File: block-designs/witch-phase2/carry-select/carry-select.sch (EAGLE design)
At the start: 12 parts, among them IC1 74AHC1G32DBV, IC2 74AHC1G08DBV, IC3 74175-S

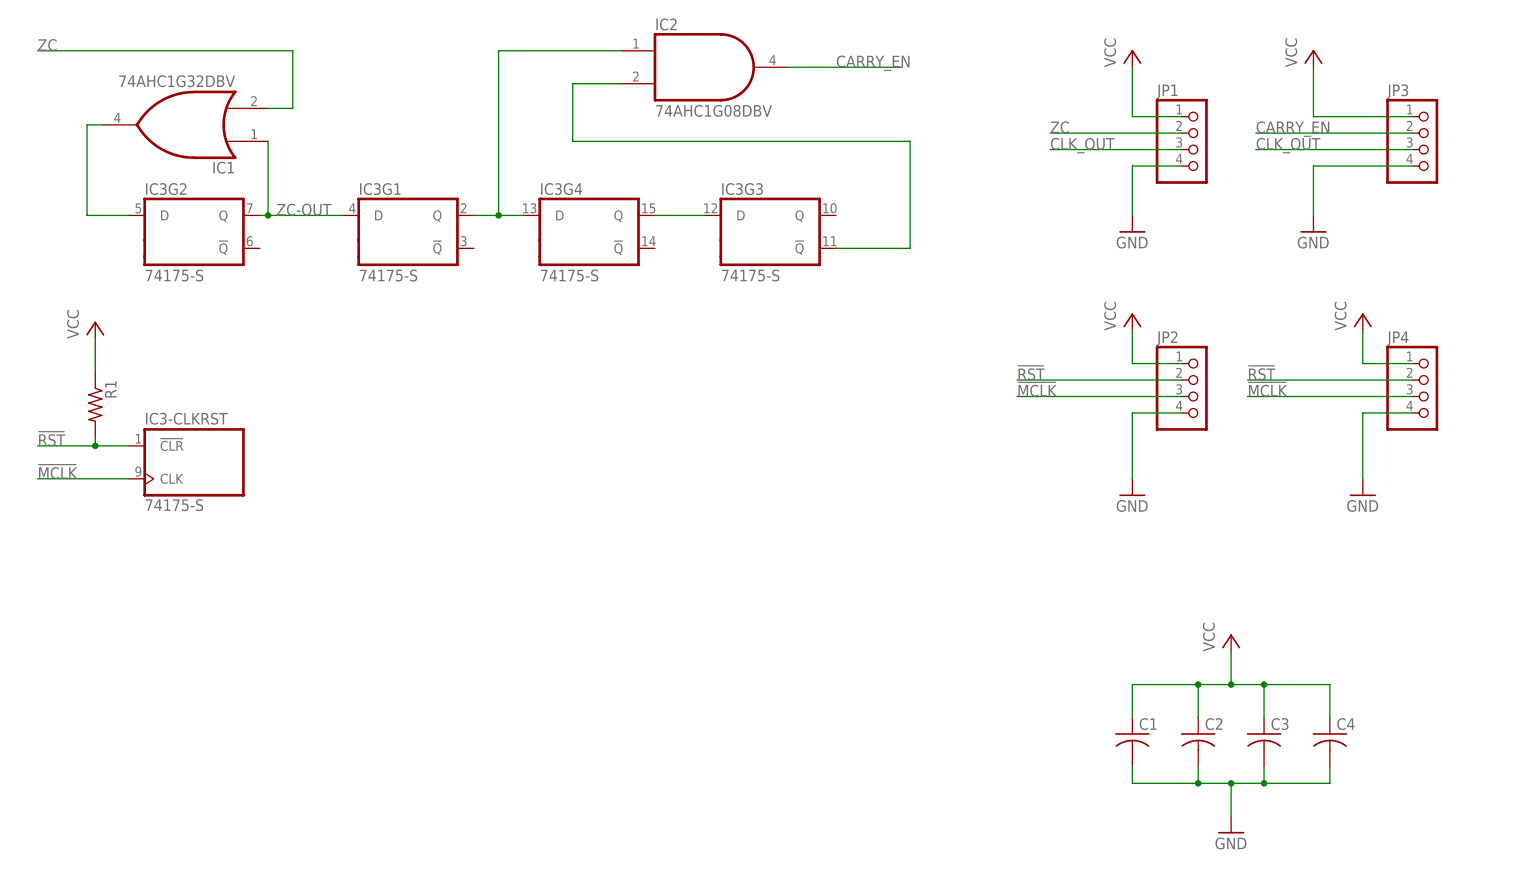
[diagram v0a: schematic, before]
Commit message: break the carry section into two pcbs and add new flipflop design
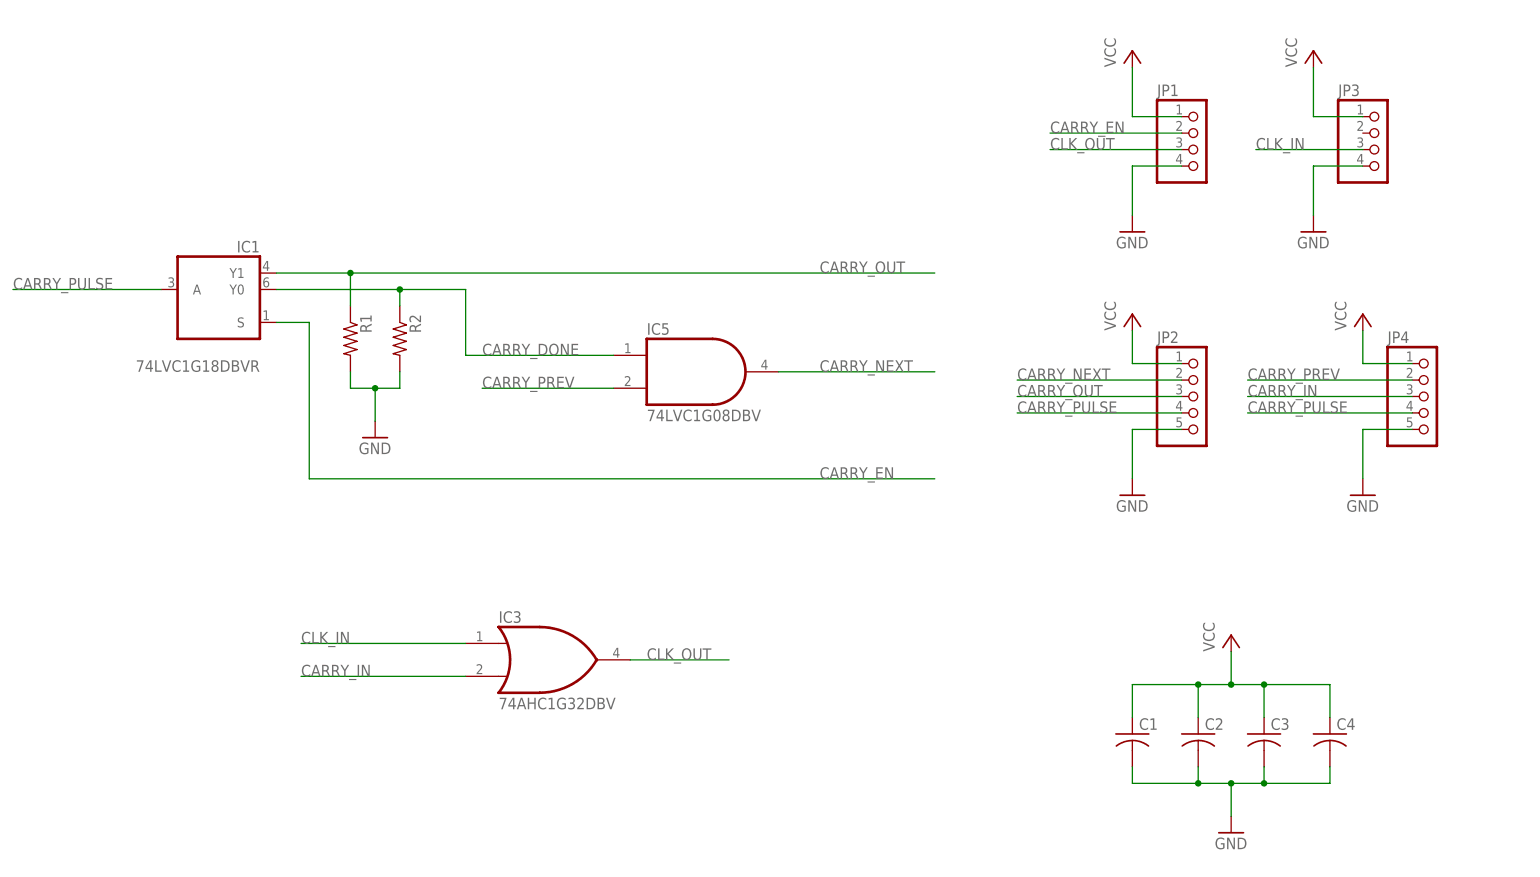
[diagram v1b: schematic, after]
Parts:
- removed IC2: 74AHC1G08DBV, 74xx-little-us:74AHC1G08DBV
- added IC5: 74LVC1G08DBV, 74xx-little-us:74LVC1G08DBV
- added R2: (no value), resistor:R-US_R0805
- IC1: value 74AHC1G32DBV -> 74LVC1G18DBVR; device 74xx-little-us:74AHC1G32DBV -> 74xx-little-us:741G18
- IC3: value 74175-S -> 74AHC1G32DBV; device 74xx-us:74175-S -> 74xx-little-us:74AHC1G32DBV
- JP2, JP4: device pinhead:PINHD-1X4 -> pinhead:PINHD-1X5
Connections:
- removed net !MCLK: IC3-CLKRST.CLK, JP2.3, JP4.3
- removed net !RST: IC3-CLKRST.!CLR, JP2.2, JP4.2, R1.2
- removed net N$1: IC2A.I0, IC3G1.Q, IC3G4.D
- removed net N$2: IC2A.I1, IC3G3.!Q
- removed net N$3: IC3G3.D, IC3G4.Q
- removed net N$5: IC1A.O, IC3G2.D
- removed net ZC: IC1A.I1, JP1.2
- removed net ZC-OUT: IC1A.I0, IC3G1.D, IC3G2.Q
- new net CARRY_DONE: IC1G$1.Y0, IC5A.I0, R2.1
- new net CARRY_IN: IC3A.I1, JP4.3
- new net CARRY_NEXT: IC5A.O, JP2.2
- new net CARRY_OUT: IC1G$1.Y1, JP2.3, R1.1
- new net CARRY_PREV: IC5A.I1, JP4.2
- new net CARRY_PULSE: IC1G$1.A, JP2.4, JP4.4
- new net CLK_IN: IC3A.I0, JP3.3
- net CARRY_EN: now also IC1G$1.S, JP1.2; no longer IC2A.O, JP3.2
- net CLK_OUT: now also IC3A.O; no longer JP3.3
- net GND: now also JP2.5, JP4.5, R1.2, R2.2; no longer JP2.4, JP4.4
- net VCC: no longer R1.1
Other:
- moved on the sheet: JP3, R1

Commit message: updated designs for new labeling and spacing
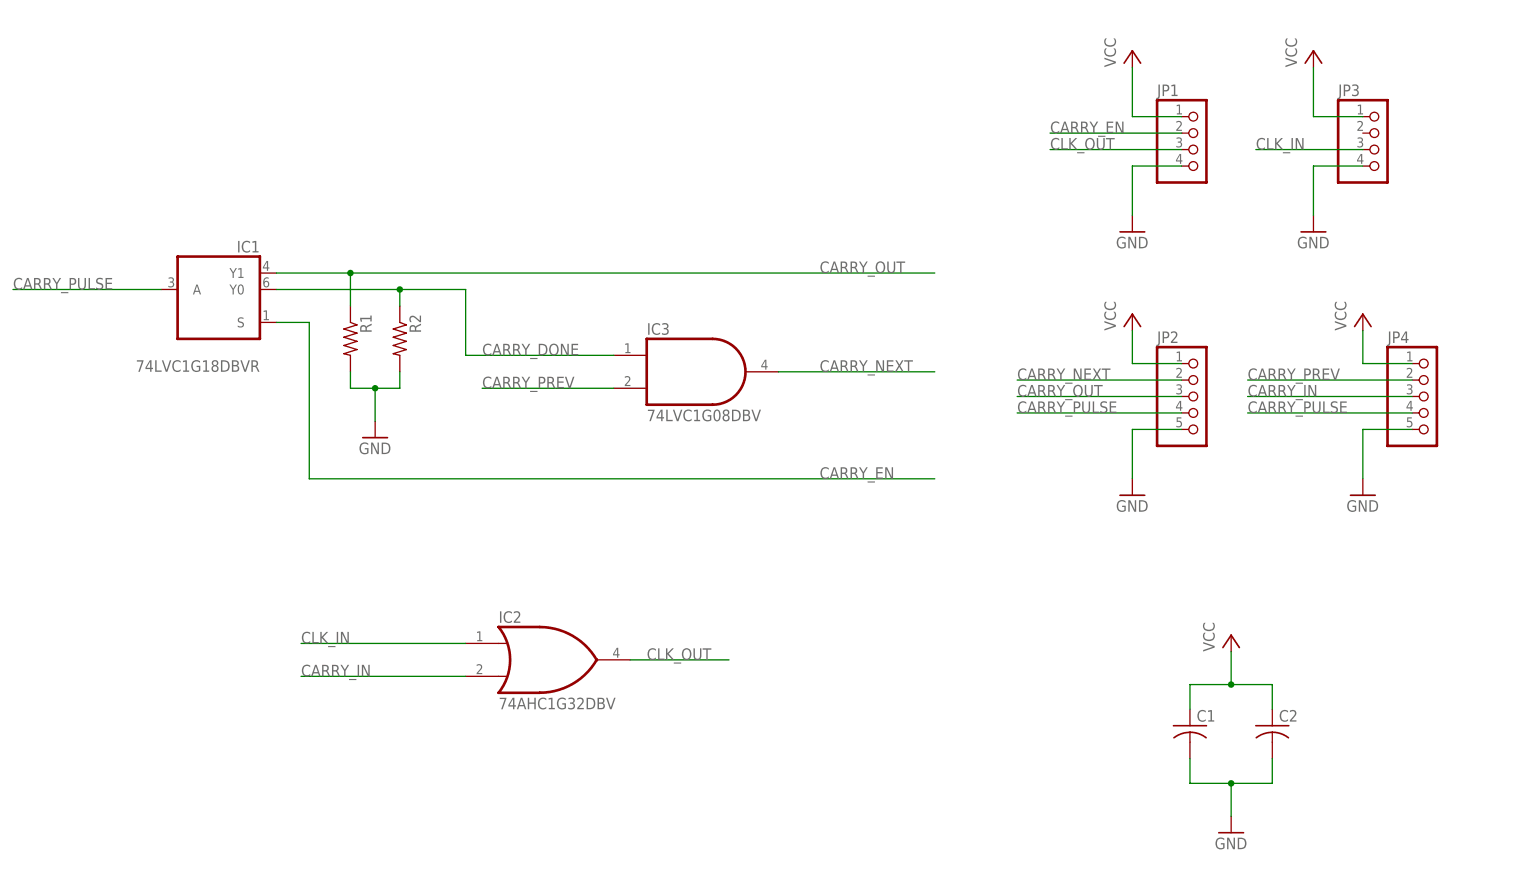
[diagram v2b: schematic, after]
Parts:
- removed C3, C4: (no value), resistor:C-USC0805
- removed IC5: 74LVC1G08DBV, 74xx-little-us:74LVC1G08DBV
- added IC2: 74AHC1G32DBV, 74xx-little-us:74AHC1G32DBV
- IC3: value 74AHC1G32DBV -> 74LVC1G08DBV; device 74xx-little-us:74AHC1G32DBV -> 74xx-little-us:74LVC1G08DBV
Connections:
- net CARRY_DONE: now also IC3A.I0; no longer IC5A.I0
- net CARRY_IN: now also IC2A.I1; no longer IC3A.I1
- net CARRY_NEXT: now also IC3A.O; no longer IC5A.O
- net CARRY_PREV: now also IC3A.I1; no longer IC5A.I1
- net CLK_IN: now also IC2A.I0; no longer IC3A.I0
- net CLK_OUT: now also IC2A.O; no longer IC3A.O
- net GND: no longer C3.2, C4.2
- net VCC: no longer C3.1, C4.1
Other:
- moved on the sheet: C1, C2
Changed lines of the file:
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@@
 <setting verticaltext="up"/>
 </settings>
-<grid distance="0.05" unitdist="inch" unit="inch" style="dots" multiple="1" display="no" altdistance="0.01" altunitdist="inch" altunit="inch"/>
+<grid distance="0.1" unitdist="inch" unit="inch" style="dots" multiple="1" display="no" altdistance="0.01" altunitdist="inch" altunit="inch"/>
 <layers>
 <layer number="1" name="Top" color="4" fill="1" visible="no" active="no"/>
@@
 <part name="GND5" library="supply1" deviceset="GND" device=""/>
 <part name="C1" library="resistor" deviceset="C-US" device="C0805"/>
+<part name="GND4" library="supply1" deviceset="GND" device=""/>
 <part name="C2" library="resistor" deviceset="C-US" device="C0805"/>
-<part name="C3" library="resistor" deviceset="C-US" device="C0805"/>
-<part name="GND4" library="supply1" deviceset="GND" device=""/>
-<part name="C4" library="resistor" deviceset="C-US" device="C0805"/>
 <part name="FRAME1" library="frames" deviceset="LETTER_L" device=""/>
 <part name="JP1" library="pinhead" deviceset="PINHD-1X4" device=""/>
@@
 <part name="JP4" library="pinhead" deviceset="PINHD-1X5" device=""/>
 <part name="IC1" library="74xx-little-us" deviceset="74*1G18" device="" value="74LVC1G18DBVR"/>
+<part name="P+3" library="supply1" deviceset="VCC" device=""/>
+<part name="P+1" library="supply1" deviceset="VCC" device=""/>
 <part name="P+4" library="supply1" deviceset="VCC" device=""/>
-<part name="P+2" library="supply1" deviceset="VCC" device=""/>
-<part name="P+5" library="supply1" deviceset="VCC" device=""/>
 <part name="R1" library="resistor" deviceset="R-US_" device="R0805"/>
 <part name="R2" library="resistor" deviceset="R-US_" device="R0805"/>
 <part name="GND1" library="supply1" deviceset="GND" device=""/>
-<part name="P+6" library="supply1" deviceset="VCC" device=""/>
-<part name="P+3" library="supply1" deviceset="VCC" device=""/>
-<part name="IC3" library="74xx-little-us" deviceset="74*1G32" device="DBV" technology="AHC"/>
-<part name="IC5" library="74xx-little-us" deviceset="74*1G08" device="DBV" technology="LVC"/>
+<part name="P+5" library="supply1" deviceset="VCC" device=""/>
+<part name="P+2" library="supply1" deviceset="VCC" device=""/>
+<part name="IC2" library="74xx-little-us" deviceset="74*1G32" device="DBV" technology="AHC"/>
+<part name="IC3" library="74xx-little-us" deviceset="74*1G08" device="DBV" technology="LVC"/>
 </parts>
 <sheets>
@@
 <instance part="GND6" gate="1" x="214.63" y="107.95"/>
 <instance part="GND5" gate="1" x="207.01" y="148.59"/>
-<instance part="C1" gate="G$1" x="179.07" y="71.12"/>
-<instance part="C2" gate="G$1" x="189.23" y="71.12"/>
-<instance part="C3" gate="G$1" x="199.39" y="71.12"/>
+<instance part="C1" gate="G$1" x="187.96" y="72.39"/>
 <instance part="GND4" gate="1" x="194.31" y="55.88"/>
-<instance part="C4" gate="G$1" x="209.55" y="71.12"/>
+<instance part="C2" gate="G$1" x="200.66" y="72.39"/>
 <instance part="FRAME1" gate="G$1" x="0" y="0"/>
 <instance part="FRAME1" gate="G$2" x="147.32" y="0"/>
@@
 <instance part="JP4" gate="A" x="224.79" y="123.19"/>
 <instance part="IC1" gate="G$1" x="38.1" y="138.43" rot="MR0"/>
-<instance part="P+4" gate="VCC" x="194.31" y="86.36"/>
-<instance part="P+2" gate="VCC" x="179.07" y="176.53"/>
-<instance part="P+5" gate="VCC" x="207.01" y="176.53"/>
+<instance part="P+3" gate="VCC" x="194.31" y="86.36"/>
+<instance part="P+1" gate="VCC" x="179.07" y="176.53"/>
+<instance part="P+4" gate="VCC" x="207.01" y="176.53"/>
 <instance part="R1" gate="G$1" x="58.42" y="132.08" rot="R270"/>
 <instance part="R2" gate="G$1" x="66.04" y="132.08" rot="R270"/>
 <instance part="GND1" gate="1" x="62.23" y="116.84"/>
-<instance part="P+6" gate="VCC" x="214.63" y="135.89"/>
-<instance part="P+3" gate="VCC" x="179.07" y="135.89"/>
-<instance part="IC3" gate="A" x="88.9" y="82.55"/>
-<instance part="IC5" gate="A" x="111.76" y="127"/>
+<instance part="P+5" gate="VCC" x="214.63" y="135.89"/>
+<instance part="P+2" gate="VCC" x="179.07" y="135.89"/>
+<instance part="IC2" gate="A" x="88.9" y="82.55"/>
+<instance part="IC3" gate="A" x="111.76" y="127"/>
 </instances>
 <busses>
@@
 </segment>
 <segment>
-<pinref part="C3" gate="G$1" pin="2"/>
-<wire x1="179.07" y1="63.5" x2="189.23" y2="63.5" width="0.1524" layer="91"/>
-<wire x1="189.23" y1="63.5" x2="194.31" y2="63.5" width="0.1524" layer="91"/>
-<wire x1="194.31" y1="63.5" x2="199.39" y2="63.5" width="0.1524" layer="91"/>
-<wire x1="199.39" y1="63.5" x2="199.39" y2="66.04" width="0.1524" layer="91"/>
+<wire x1="187.96" y1="63.5" x2="194.31" y2="63.5" width="0.1524" layer="91"/>
 <pinref part="C1" gate="G$1" pin="2"/>
-<wire x1="179.07" y1="66.04" x2="179.07" y2="63.5" width="0.1524" layer="91"/>
+<wire x1="187.96" y1="67.31" x2="187.96" y2="63.5" width="0.1524" layer="91"/>
 <pinref part="C2" gate="G$1" pin="2"/>
-<wire x1="189.23" y1="66.04" x2="189.23" y2="63.5" width="0.1524" layer="91"/>
-<pinref part="C4" gate="G$1" pin="2"/>
-<wire x1="209.55" y1="66.04" x2="209.55" y2="63.5" width="0.1524" layer="91"/>
-<wire x1="209.55" y1="63.5" x2="199.39" y2="63.5" width="0.1524" layer="91"/>
-<junction x="199.39" y="63.5"/>
-<junction x="189.23" y="63.5"/>
+<wire x1="200.66" y1="67.31" x2="200.66" y2="63.5" width="0.1524" layer="91"/>
+<wire x1="200.66" y1="63.5" x2="194.31" y2="63.5" width="0.1524" layer="91"/>
 <pinref part="GND4" gate="1" pin="GND"/>
 <wire x1="194.31" y1="58.42" x2="194.31" y2="63.5" width="0.1524" layer="91"/>
@@
 <junction x="66.04" y="139.7"/>
 <label x="78.74" y="129.54" size="1.778" layer="95"/>
-<pinref part="IC5" gate="A" pin="I0"/>
+<pinref part="IC3" gate="A" pin="I0"/>
 <wire x1="99.06" y1="129.54" x2="76.2" y2="129.54" width="0.1524" layer="91"/>
 <wire x1="76.2" y1="129.54" x2="76.2" y2="139.7" width="0.1524" layer="91"/>
@@
 <net name="VCC" class="0">
 <segment>
-<pinref part="C3" gate="G$1" pin="1"/>
-<wire x1="179.07" y1="78.74" x2="189.23" y2="78.74" width="0.1524" layer="91"/>
-<wire x1="189.23" y1="78.74" x2="194.31" y2="78.74" width="0.1524" layer="91"/>
-<wire x1="194.31" y1="78.74" x2="199.39" y2="78.74" width="0.1524" layer="91"/>
-<wire x1="199.39" y1="78.74" x2="199.39" y2="73.66" width="0.1524" layer="91"/>
+<wire x1="187.96" y1="78.74" x2="194.31" y2="78.74" width="0.1524" layer="91"/>
 <pinref part="C1" gate="G$1" pin="1"/>
-<wire x1="179.07" y1="73.66" x2="179.07" y2="78.74" width="0.1524" layer="91"/>
+<wire x1="187.96" y1="74.93" x2="187.96" y2="78.74" width="0.1524" layer="91"/>
 <pinref part="C2" gate="G$1" pin="1"/>
-<wire x1="189.23" y1="73.66" x2="189.23" y2="78.74" width="0.1524" layer="91"/>
-<pinref part="C4" gate="G$1" pin="1"/>
-<wire x1="199.39" y1="78.74" x2="209.55" y2="78.74" width="0.1524" layer="91"/>
-<wire x1="209.55" y1="78.74" x2="209.55" y2="73.66" width="0.1524" layer="91"/>
-<junction x="189.23" y="78.74"/>
-<junction x="199.39" y="78.74"/>
+<wire x1="194.31" y1="78.74" x2="200.66" y2="78.74" width="0.1524" layer="91"/>
+<wire x1="200.66" y1="78.74" x2="200.66" y2="74.93" width="0.1524" layer="91"/>
 <wire x1="194.31" y1="78.74" x2="194.31" y2="83.82" width="0.1524" layer="91"/>
 <junction x="194.31" y="78.74"/>
-<pinref part="P+4" gate="VCC" pin="VCC"/>
+<pinref part="P+3" gate="VCC" pin="VCC"/>
 </segment>
 <segment>
@@
 <wire x1="179.07" y1="166.37" x2="179.07" y2="173.99" width="0.1524" layer="91"/>
 <pinref part="JP1" gate="A" pin="1"/>
-<pinref part="P+2" gate="VCC" pin="VCC"/>
+<pinref part="P+1" gate="VCC" pin="VCC"/>
 </segment>
 <segment>
@@
 <wire x1="207.01" y1="166.37" x2="207.01" y2="173.99" width="0.1524" layer="91"/>
 <pinref part="JP3" gate="A" pin="1"/>
-<pinref part="P+5" gate="VCC" pin="VCC"/>
+<pinref part="P+4" gate="VCC" pin="VCC"/>
 </segment>
 <segment>
@@
 <wire x1="222.25" y1="128.27" x2="214.63" y2="128.27" width="0.1524" layer="91"/>
 <wire x1="214.63" y1="128.27" x2="214.63" y2="133.35" width="0.1524" layer="91"/>
-<pinref part="P+6" gate="VCC" pin="VCC"/>
+<pinref part="P+5" gate="VCC" pin="VCC"/>
 </segment>
 <segment>
@@
 <wire x1="186.69" y1="128.27" x2="179.07" y2="128.27" width="0.1524" layer="91"/>
 <wire x1="179.07" y1="128.27" x2="179.07" y2="133.35" width="0.1524" layer="91"/>
-<pinref part="P+3" gate="VCC" pin="VCC"/>
+<pinref part="P+2" gate="VCC" pin="VCC"/>
 </segment>
 </net>
@@
 </segment>
 <segment>
-<pinref part="IC3" gate="A" pin="I0"/>
+<pinref part="IC2" gate="A" pin="I0"/>
 <wire x1="76.2" y1="85.09" x2="50.8" y2="85.09" width="0.1524" layer="91"/>
 <label x="50.8" y="85.09" size="1.778" layer="95"/>
@@
 </segment>
 <segment>
-<pinref part="IC3" gate="A" pin="O"/>
+<pinref part="IC2" gate="A" pin="O"/>
 <wire x1="101.6" y1="82.55" x2="116.84" y2="82.55" width="0.1524" layer="91"/>
 <label x="104.14" y="82.55" size="1.778" layer="95"/>
@@
 </segment>
 <segment>
-<pinref part="IC5" gate="A" pin="O"/>
+<pinref part="IC3" gate="A" pin="O"/>
 <wire x1="124.46" y1="127" x2="148.59" y2="127" width="0.1524" layer="91"/>
 <label x="130.81" y="127" size="1.778" layer="95"/>
@@
 </segment>
 <segment>
-<pinref part="IC5" gate="A" pin="I1"/>
+<pinref part="IC3" gate="A" pin="I1"/>
 <wire x1="99.06" y1="124.46" x2="78.74" y2="124.46" width="0.1524" layer="91"/>
 <label x="78.74" y="124.46" size="1.778" layer="95"/>
@@
 <net name="CARRY_IN" class="0">
 <segment>
-<pinref part="IC3" gate="A" pin="I1"/>
+<pinref part="IC2" gate="A" pin="I1"/>
 <wire x1="76.2" y1="80.01" x2="50.8" y2="80.01" width="0.1524" layer="91"/>
 <label x="50.8" y="80.01" size="1.778" layer="95"/>
